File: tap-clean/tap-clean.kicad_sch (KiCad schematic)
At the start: 14 parts, among them J4 Barrel_Jack_Switch, U1 74HC595

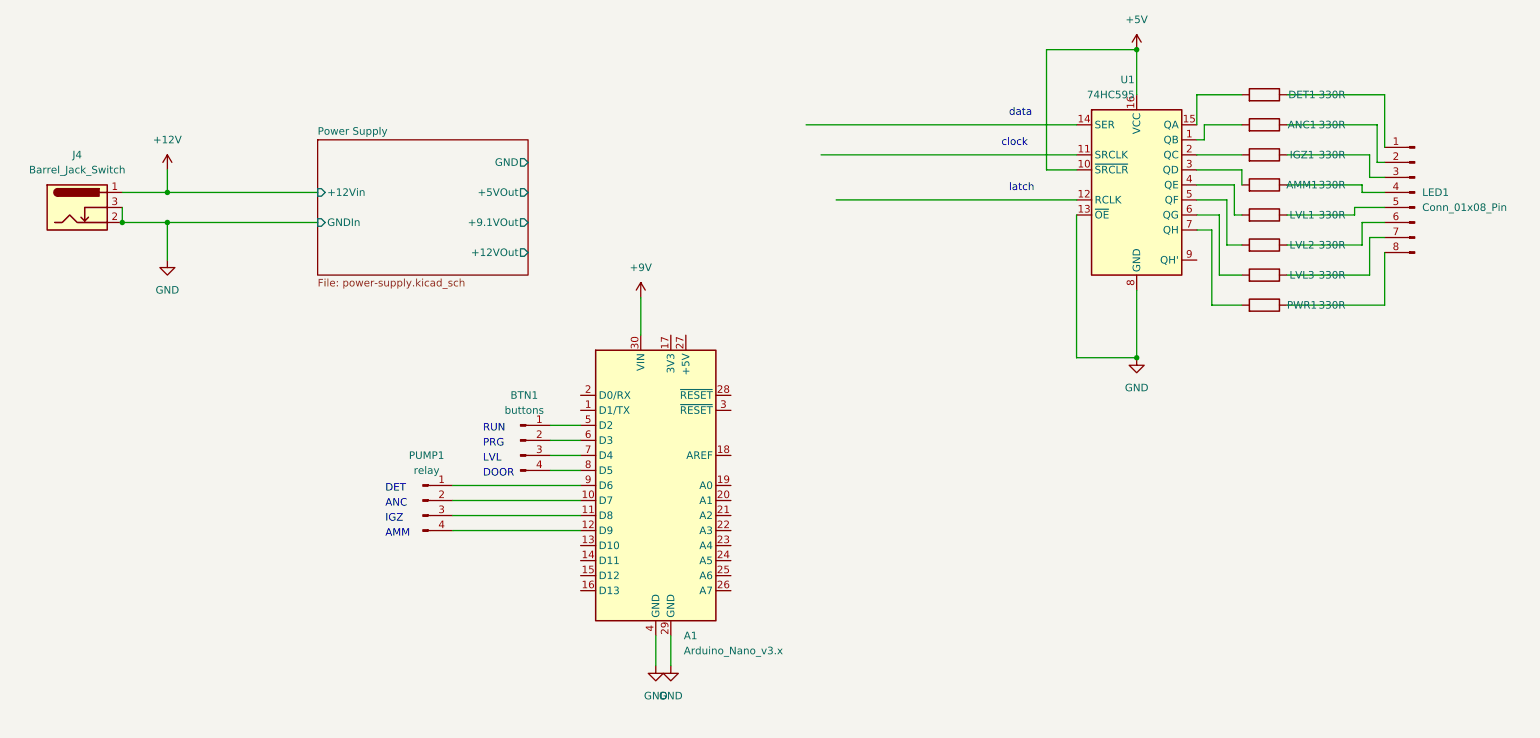
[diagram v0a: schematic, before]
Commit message: adding footprint to connections
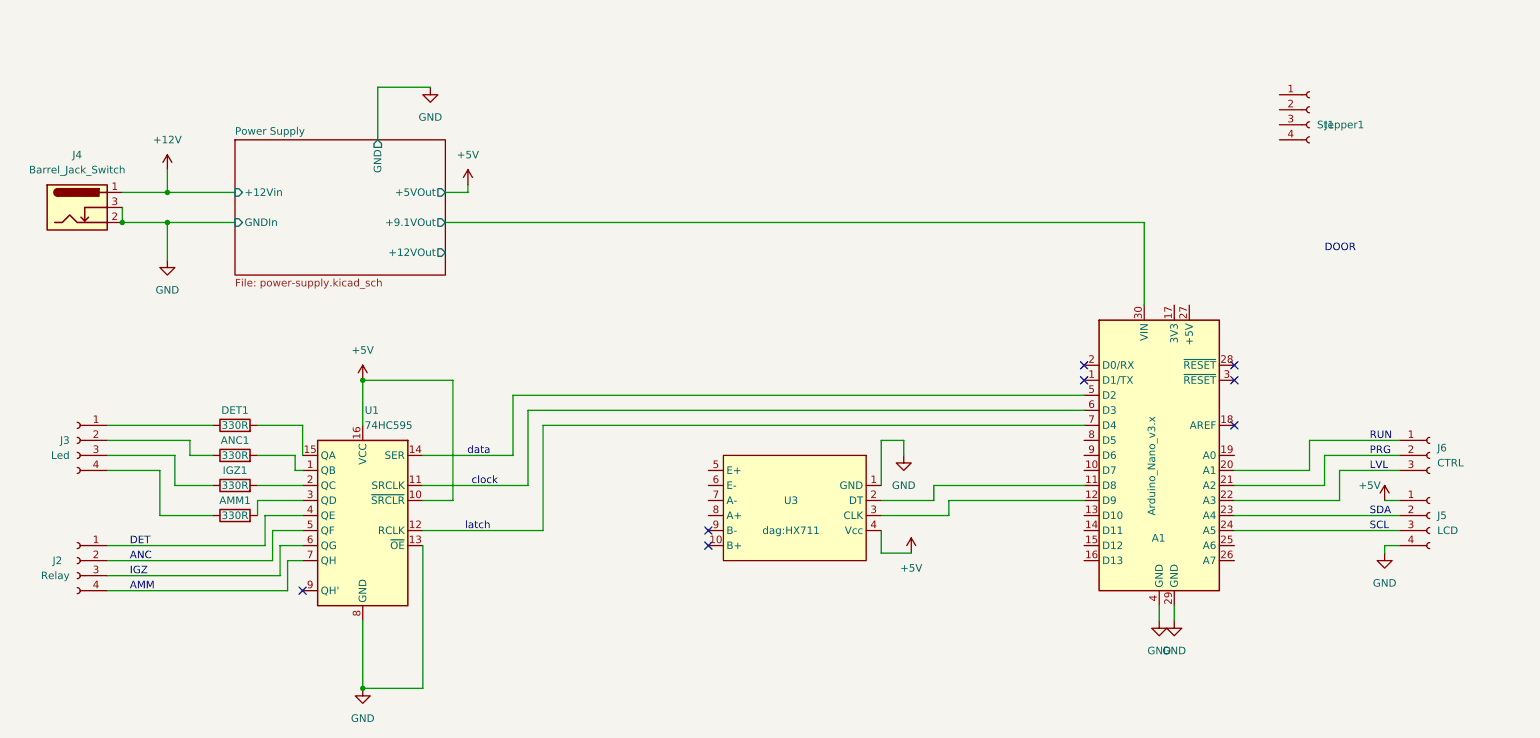
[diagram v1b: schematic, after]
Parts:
- removed BTN1: buttons, Connector_PinHeader_2.54mm:PinHeader_1x04_P2.54mm_Vertical, symbol Connector:Conn_01x04_Pin
- removed LED1: Conn_01x08_Pin, Connector_PinHeader_2.54mm:PinHeader_1x08_P2.54mm_Vertical, symbol Connector:Conn_01x08_Pin
- removed LVL1, LVL2, LVL3, PWR1: 330R, Resistor_THT:R_Axial_DIN0207_L6.3mm_D2.5mm_P10.16mm_Horizontal, symbol Device:R
- removed PUMP1: relay, Connector_PinHeader_2.54mm:PinHeader_1x04_P2.54mm_Vertical, symbol Connector:Conn_01x04_Pin
- added J1: Stepper1, Connector_JST:JST_XH_B4B-XH-A_1x04_P2.50mm_Vertical, symbol Connector:Conn_01x04_Socket
- added J2: Relay, Connector_JST:JST_XH_B4B-XH-A_1x04_P2.50mm_Vertical, symbol Connector:Conn_01x04_Socket
- added J3: Led, Connector_JST:JST_XH_B4B-XH-A_1x04_P2.50mm_Vertical, symbol Connector:Conn_01x04_Socket
- added J5: LCD, Connector_JST:JST_XH_B4B-XH-A_1x04_P2.50mm_Vertical, symbol Connector:Conn_01x04_Socket
- added J6: CTRL, Connector_JST:JST_XH_B3B-XH-A_1x03_P2.50mm_Vertical, symbol Connector:Conn_01x03_Socket
- added U3: ~, dag:HX711, symbol dag1:HX711
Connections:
- net +9V is gone; now on net Power Supply/+9.1VOut: A1.30 (VIN)
- net +5V: now also J5.1 (Pin_1), U3.4 (Vcc)
- net GND: now also J5.4 (Pin_4), U3.1 (GND)
- net at A1.11 (D8): now also U3.2 (DT)
- net at A1.12 (D9): now also U3.3 (CLK)
- net at AMM1.1: now also J3.4 (Pin_4)
- net at ANC1.1: now also J3.2 (Pin_2)
- net at U1.4 (QE): now also J2.1 (Pin_1)
- net at U1.11 (SRCLK): now also A1.6 (D3)
- net at U1.12 (RCLK): now also A1.7 (D4)
- net at U1.14 (SER): now also A1.5 (D2)
- net at U1.5 (QF): now also J2.2 (Pin_2)
- net at U1.6 (QG): now also J2.3 (Pin_3)
- net at U1.7 (QH): now also J2.4 (Pin_4)
- net at DET1.1: now also J3.1 (Pin_1)
- net at IGZ1.1: now also J3.3 (Pin_3)
- net at A1.20 (A1): now also J6.1 (Pin_1)
- net at A1.21 (A2): now also J6.2 (Pin_2)
- net at A1.22 (A3): now also J6.3 (Pin_3)
- net at A1.23 (A4): now also J5.2 (Pin_2)
- net at A1.24 (A5): now also J5.3 (Pin_3)
- no-connect marks 0 -> 8
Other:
- note added: "SCL"
- note added: "SDA"
- moved on the sheet: A1, AMM1, ANC1, DET1, IGZ1, U1
